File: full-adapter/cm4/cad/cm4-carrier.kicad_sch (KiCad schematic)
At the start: 0 parts

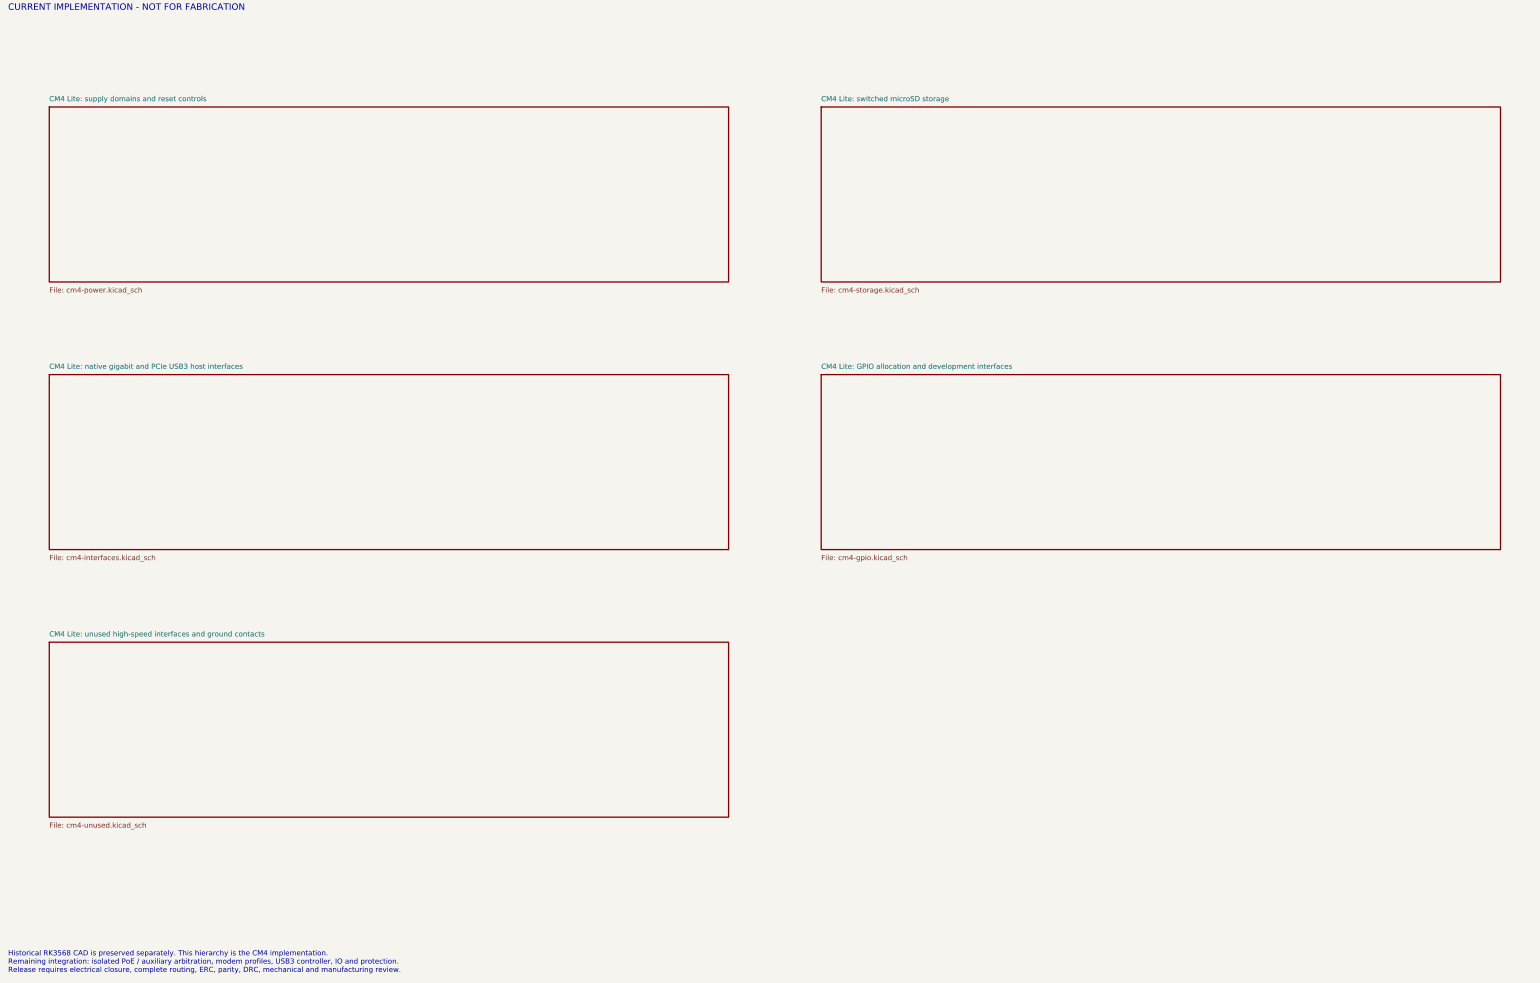
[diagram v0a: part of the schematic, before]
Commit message: Capture CM4 gigabit magnetics and isolated PoE termination
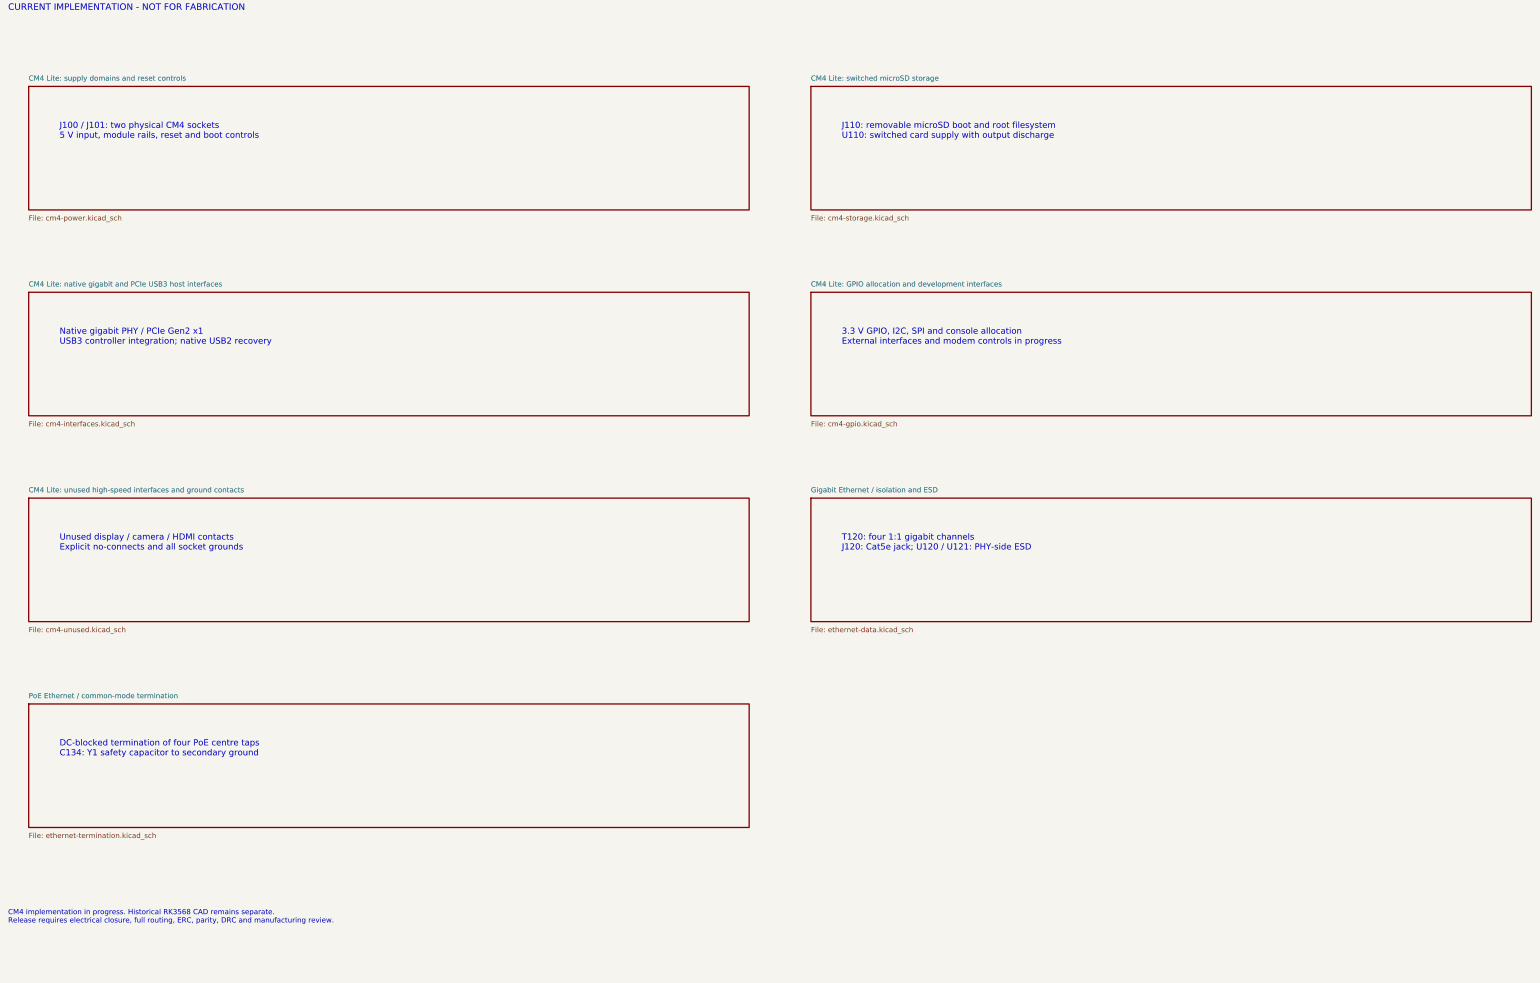
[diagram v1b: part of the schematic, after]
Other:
- added sheet Gigabit Ethernet / isolation and ESD (ethernet-data.kicad_sch)
- added sheet PoE Ethernet / common-mode termination (ethernet-termination.kicad_sch)
- note added: "3.3 V GPIO, I2C, SPI and console allocation External interfaces and modem controls in progress"
- note added: "CM4 implementation in progress. Historical RK3568 CAD remains separate. Release requires electrical closure, full routing, ERC, parity, DRC and manufacturing review."
- note added: "DC-blocked termination of four PoE centre taps C134: Y1 safety capacitor to secondary ground"
- note added: "J100 / J101: two physical CM4 sockets 5 V input, module rails, reset and boot controls"
- note added: "J110: removable microSD boot and root filesystem U110: switched card supply with output discharge"
- note added: "Native gigabit PHY / PCIe Gen2 x1 USB3 controller integration; native USB2 recovery"
- note added: "T120: four 1:1 gigabit channels J120: Cat5e jack; U120 / U121: PHY-side ESD"
- note added: "Unused display / camera / HDMI contacts Explicit no-connects and all socket grounds"
- note removed: "Historical RK3568 CAD is preserved separately. This hierarchy is the CM4 implementation. Remaining integration: isolated PoE / auxiliary arbitration, modem profiles, USB3 controller, IO and protection. Release requires electrical closure, complete routing, ERC, parity, DRC, mechanical and manufacturing review."
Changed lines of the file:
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@@
 (text "CM4001000 / 1 GB Lite / native gigabit / PCIe USB3 / isolated PoE" (at 15.24 15.24 0) (effects (font (size 2.0 2.0)) (justify left top)))
 (text "CURRENT IMPLEMENTATION - NOT FOR FABRICATION" (at 15.24 25.4 0) (effects (font (size 1.6 1.6)) (justify left top)))
-(sheet (at 25.4 50.8) (size 167.64 43.18) (stroke (width 0.254) (type default)) (fill (color 0 0 0 0)) (property "Sheetname" "CM4 Lite: supply domains and reset controls" (at 25.4 49.529999999999994 0) (effects (font (size 1.27 1.27)) (justify left bottom))) (property "Sheetfile" "cm4-power.kicad_sch" (at 25.4 95.25 0) (effects (font (size 1.27 1.27)) (justify left top))) (instances (project "cm4-carrier" (path "/a9c717cf-0889-5108-86c7-e85b9dbb05bc" (page "2")))))
-(sheet (at 215.9 50.8) (size 167.64 43.18) (stroke (width 0.254) (type default)) (fill (color 0 0 0 0)) (property "Sheetname" "CM4 Lite: switched microSD storage" (at 215.9 49.529999999999994 0) (effects (font (size 1.27 1.27)) (justify left bottom))) (property "Sheetfile" "cm4-storage.kicad_sch" (at 215.9 95.25 0) (effects (font (size 1.27 1.27)) (justify left top))) (instances (project "cm4-carrier" (path "/a9c717cf-0889-5108-86c7-e85b9dbb05bc" (page "3")))))
-(sheet (at 25.4 116.84) (size 167.64 43.18) (stroke (width 0.254) (type default)) (fill (color 0 0 0 0)) (property "Sheetname" "CM4 Lite: native gigabit and PCIe USB3 host interfaces" (at 25.4 115.57000000000001 0) (effects (font (size 1.27 1.27)) (justify left bottom))) (property "Sheetfile" "cm4-interfaces.kicad_sch" (at 25.4 161.29000000000002 0) (effects (font (size 1.27 1.27)) (justify left top))) (instances (project "cm4-carrier" (path "/a9c717cf-0889-5108-86c7-e85b9dbb05bc" (page "4")))))
-(sheet (at 215.9 116.84) (size 167.64 43.18) (stroke (width 0.254) (type default)) (fill (color 0 0 0 0)) (property "Sheetname" "CM4 Lite: GPIO allocation and development interfaces" (at 215.9 115.57000000000001 0) (effects (font (size 1.27 1.27)) (justify left bottom))) (property "Sheetfile" "cm4-gpio.kicad_sch" (at 215.9 161.29000000000002 0) (effects (font (size 1.27 1.27)) (justify left top))) (instances (project "cm4-carrier" (path "/a9c717cf-0889-5108-86c7-e85b9dbb05bc" (page "5")))))
-(sheet (at 25.4 182.88) (size 167.64 43.18) (stroke (width 0.254) (type default)) (fill (color 0 0 0 0)) (property "Sheetname" "CM4 Lite: unused high-speed interfaces and ground contacts" (at 25.4 181.60999999999999 0) (effects (font (size 1.27 1.27)) (justify left bottom))) (property "Sheetfile" "cm4-unused.kicad_sch" (at 25.4 227.32999999999998 0) (effects (font (size 1.27 1.27)) (justify left top))) (instances (project "cm4-carrier" (path "/a9c717cf-0889-5108-86c7-e85b9dbb05bc" (page "6")))))
-(text "Historical RK3568 CAD is preserved separately. This hierarchy is the CM4 implementation.\nRemaining integration: isolated PoE / auxiliary arbitration, modem profiles, USB3 controller, IO and protection.\nRelease requires electrical closure, complete routing, ERC, parity, DRC, mechanical and manufacturing review." (at 15.24 259.08 0) (effects (font (size 1.27 1.27)) (justify left top)))
+(sheet (at 20.32 45.72) (size 177.8 30.48) (stroke (width 0.254) (type default)) (fill (color 0 0 0 0)) (property "Sheetname" "CM4 Lite: supply domains and reset controls" (at 20.32 44.449999999999996 0) (effects (font (size 1.27 1.27)) (justify left bottom))) (property "Sheetfile" "cm4-power.kicad_sch" (at 20.32 77.47 0) (effects (font (size 1.27 1.27)) (justify left top))) (instances (project "cm4-carrier" (path "/a9c717cf-0889-5108-86c7-e85b9dbb05bc" (page "2")))))
+(text "J100 / J101: two physical CM4 sockets\n5 V input, module rails, reset and boot controls" (at 27.94 54.61 0) (effects (font (size 1.52 1.52)) (justify left top)))
+(sheet (at 213.35999999999999 45.72) (size 177.8 30.48) (stroke (width 0.254) (type default)) (fill (color 0 0 0 0)) (property "Sheetname" "CM4 Lite: switched microSD storage" (at 213.35999999999999 44.449999999999996 0) (effects (font (size 1.27 1.27)) (justify left bottom))) (property "Sheetfile" "cm4-storage.kicad_sch" (at 213.35999999999999 77.47 0) (effects (font (size 1.27 1.27)) (justify left top))) (instances (project "cm4-carrier" (path "/a9c717cf-0889-5108-86c7-e85b9dbb05bc" (page "3")))))
+(text "J110: removable microSD boot and root filesystem\nU110: switched card supply with output discharge" (at 220.98 54.61 0) (effects (font (size 1.52 1.52)) (justify left top)))
+(sheet (at 20.32 96.52) (size 177.8 30.48) (stroke (width 0.254) (type default)) (fill (color 0 0 0 0)) (property "Sheetname" "CM4 Lite: native gigabit and PCIe USB3 host interfaces" (at 20.32 95.25 0) (effects (font (size 1.27 1.27)) (justify left bottom))) (property "Sheetfile" "cm4-interfaces.kicad_sch" (at 20.32 128.26999999999998 0) (effects (font (size 1.27 1.27)) (justify left top))) (instances (project "cm4-carrier" (path "/a9c717cf-0889-5108-86c7-e85b9dbb05bc" (page "4")))))
+(text "Native gigabit PHY / PCIe Gen2 x1\nUSB3 controller integration; native USB2 recovery" (at 27.94 105.41 0) (effects (font (size 1.52 1.52)) (justify left top)))
+(sheet (at 213.35999999999999 96.52) (size 177.8 30.48) (stroke (width 0.254) (type default)) (fill (color 0 0 0 0)) (property "Sheetname" "CM4 Lite: GPIO allocation and development interfaces" (at 213.35999999999999 95.25 0) (effects (font (size 1.27 1.27)) (justify left bottom))) (property "Sheetfile" "cm4-gpio.kicad_sch" (at 213.35999999999999 128.26999999999998 0) (effects (font (size 1.27 1.27)) (justify left top))) (instances (project "cm4-carrier" (path "/a9c717cf-0889-5108-86c7-e85b9dbb05bc" (page "5")))))
+(text "3.3 V GPIO, I2C, SPI and console allocation\nExternal interfaces and modem controls in progress" (at 220.98 105.41 0) (effects (font (size 1.52 1.52)) (justify left top)))
+(sheet (at 20.32 147.32) (size 177.8 30.48) (stroke (width 0.254) (type default)) (fill (color 0 0 0 0)) (property "Sheetname" "CM4 Lite: unused high-speed interfaces and ground contacts" (at 20.32 146.04999999999998 0) (effects (font (size 1.27 1.27)) (justify left bottom))) (property "Sheetfile" "cm4-unused.kicad_sch" (at 20.32 179.07 0) (effects (font (size 1.27 1.27)) (justify left top))) (instances (project "cm4-carrier" (path "/a9c717cf-0889-5108-86c7-e85b9dbb05bc" (page "6")))))
+(text "Unused display / camera / HDMI contacts\nExplicit no-connects and all socket grounds" (at 27.94 156.20999999999998 0) (effects (font (size 1.52 1.52)) (justify left top)))
+(sheet (at 213.35999999999999 147.32) (size 177.8 30.48) (stroke (width 0.254) (type default)) (fill (color 0 0 0 0)) (property "Sheetname" "Gigabit Ethernet / isolation and ESD" (at 213.35999999999999 146.04999999999998 0) (effects (font (size 1.27 1.27)) (justify left bottom))) (property "Sheetfile" "ethernet-data.kicad_sch" (at 213.35999999999999 179.07 0) (effects (font (size 1.27 1.27)) (justify left top))) (instances (project "cm4-carrier" (path "/a9c717cf-0889-5108-86c7-e85b9dbb05bc" (page "7")))))
+(text "T120: four 1:1 gigabit channels\nJ120: Cat5e jack; U120 / U121: PHY-side ESD" (at 220.98 156.20999999999998 0) (effects (font (size 1.52 1.52)) (justify left top)))
+(sheet (at 20.32 198.11999999999998) (size 177.8 30.48) (stroke (width 0.254) (type default)) (fill (color 0 0 0 0)) (property "Sheetname" "PoE Ethernet / common-mode termination" (at 20.32 196.84999999999997 0) (effects (font (size 1.27 1.27)) (justify left bottom))) (property "Sheetfile" "ethernet-termination.kicad_sch" (at 20.32 229.86999999999998 0) (effects (font (size 1.27 1.27)) (justify left top))) (instances (project "cm4-carrier" (path "/a9c717cf-0889-5108-86c7-e85b9dbb05bc" (page "8")))))
+(text "DC-blocked termination of four PoE centre taps\nC134: Y1 safety capacitor to secondary ground" (at 27.94 207.01 0) (effects (font (size 1.52 1.52)) (justify left top)))
+(text "CM4 implementation in progress. Historical RK3568 CAD remains separate.\nRelease requires electrical closure, full routing, ERC, parity, DRC and manufacturing review." (at 15.24 248.92 0) (effects (font (size 1.27 1.27)) (justify left top)))
 )

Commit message: Capture CM4 USB-C power input and source arbitration
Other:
- added sheet Power input arbitration (input-mux.kicad_sch)
- added sheet USB-C: PD and housekeeping (aux-pd.kicad_sch)
- added sheet USB-C: connector and protection (aux-usbc.kicad_sch)
- added sheet USB-C: voltage qualification (aux-window.kicad_sch)
- note added: "J150: power-only USB-C input U151: CC protection and dead-battery Rd"
- note added: "U150: fixed 20 V / 3 A PD request U152: independent auxiliary housekeeping"
- note added: "U153: precise auxiliary voltage qualification Hardware disconnect on voltage or CC fault"
- note added: "U160: independent reverse blocking Only qualified inputs may power VIN_SYS"

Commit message: Capture CM4 modem profiles and protected SIM interfaces
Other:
- added sheet Modem: SIM1 and SIM2 profile links (modem-sim-profile.kicad_sch)
- added sheet Modem: USB3 and vendor detection (modem-usb.kicad_sch)
- added sheet Modem: controls and reserved contacts (modem-signals.kicad_sch)
- added sheet Modem: socket power and profiles (modem-power.kicad_sch)
- added sheet SIM1: protected nano-SIM socket (sim1.kicad_sch)
- added sheet SIM2: protected nano-SIM socket (sim2.kicad_sch)
- note added: "Independent power / reset / radio endpoints Unused PCIe and reserved contacts"
- note added: "J200: 1 A/contact B-key modem socket Sierra-only extra supply contacts"
- note added: "J201: protected nano-SIM1 Module-powered, normally closed detection"
- note added: "J202: optional external nano-SIM2 All five profile links default absent"
- note added: "SIM1 common; SIM2 physically isolated EM9190 mmWave / Quectel eSIM boundaries"
- note added: "USB3 pairs and USB2 companion Sierra-only detection and interface selection"
